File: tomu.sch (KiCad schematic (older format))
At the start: 14 parts, among them P1 DEBUG, P3 USB-PCB, U1 MKL27Z256VFM4

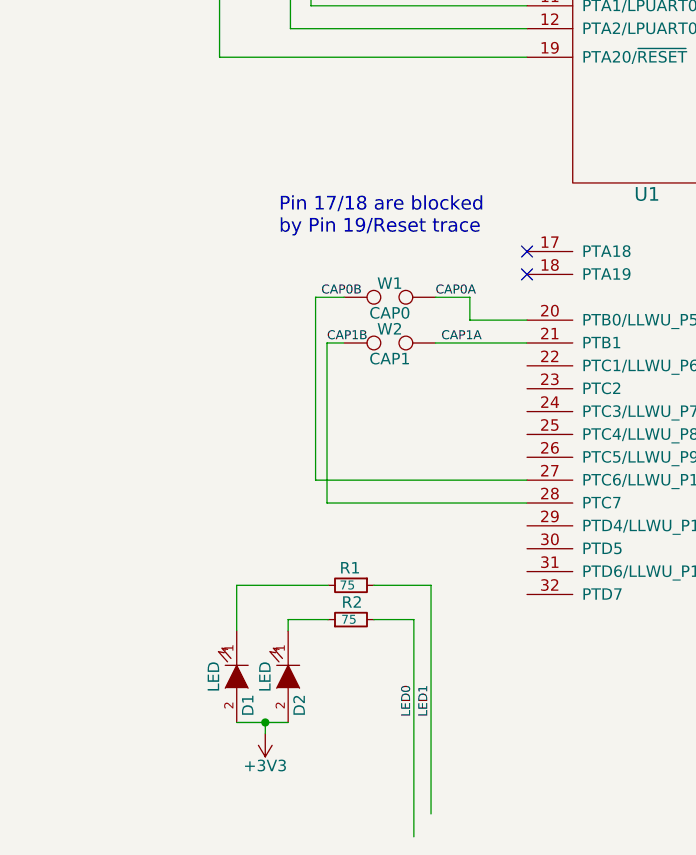
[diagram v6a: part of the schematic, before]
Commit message: Adding atecc508a part.
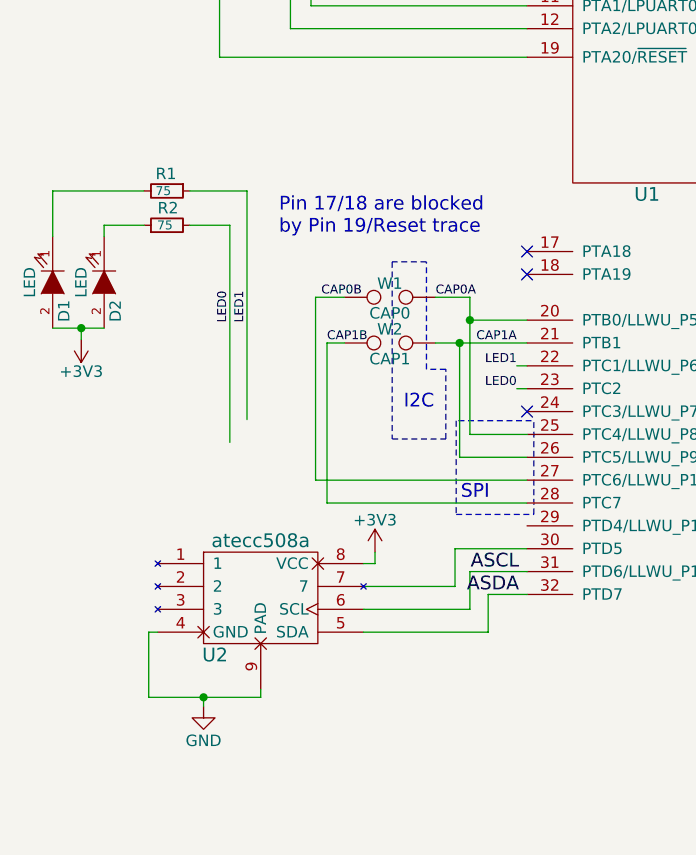
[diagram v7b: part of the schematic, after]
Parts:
- added U2: atecc508a, Housings_DFN_QFN:DFN-8-1EP_3x2mm_Pitch0.5mm, symbol atecc508a
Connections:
- net labels added: ASCL, ASDA
- wire segments 64 -> 85
- no-connect marks 2 -> 3
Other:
- note added: "I2C"
- note added: "SPI"
- moved on the sheet: D1, D2, R1, R2
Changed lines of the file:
@@
 LIBS:mkl27z265vfm4
 LIBS:usb-pcb
+LIBS:atecc508a
 LIBS:tomu-cache
 EELAYER 25 0
@@
 L LED D1
 U 1 1 5798F0D5
-P 1665 5235
-F 0 "D1" H 1790 5285 50  0000 C CNN
-F 1 "LED" H 1665 5135 50  0000 C CNN
-F 2 "LEDs:LED_0402" H 1665 5235 50  0001 C CNN
-F 3 "" H 1665 5235 50  0000 C CNN
-	1    1665 5235
+P 860 3510
+F 0 "D1" H 985 3560 50  0000 C CNN
+F 1 "LED" H 860 3410 50  0000 C CNN
+F 2 "LEDs:LED_0402" H 860 3510 50  0001 C CNN
+F 3 "" H 860 3510 50  0000 C CNN
+	1    860  3510
 	0    1    1    0
 $EndComp
@@
 L LED D2
 U 1 1 5798F173
-P 1890 5235
-F 0 "D2" H 2015 5285 50  0000 C CNN
-F 1 "LED" H 1890 5135 50  0000 C CNN
-F 2 "LEDs:LED_0402" H 1890 5235 50  0001 C CNN
-F 3 "" H 1890 5235 50  0000 C CNN
-	1    1890 5235
+P 1085 3510
+F 0 "D2" H 1210 3560 50  0000 C CNN
+F 1 "LED" H 1085 3410 50  0000 C CNN
+F 2 "LEDs:LED_0402" H 1085 3510 50  0001 C CNN
+F 3 "" H 1085 3510 50  0000 C CNN
+	1    1085 3510
 	0    1    1    0
 $EndComp
@@
 L R_Small R2
 U 1 1 5798F38A
-P 2165 4985
-F 0 "R2" V 2240 4935 50  0000 L CNN
-F 1 "75" V 2165 4960 39  0000 L CNN
-F 2 "Resistors_SMD:R_0402" H 2165 4985 50  0001 C CNN
-F 3 "" H 2165 4985 50  0000 C CNN
-	1    2165 4985
+P 1360 3260
+F 0 "R2" V 1435 3210 50  0000 L CNN
+F 1 "75" V 1360 3235 39  0000 L CNN
+F 2 "Resistors_SMD:R_0402" H 1360 3260 50  0001 C CNN
+F 3 "" H 1360 3260 50  0000 C CNN
+	1    1360 3260
 	0    -1   -1   0
 $EndComp
@@
 L R_Small R1
 U 1 1 5798F3FD
-P 2165 4835
-F 0 "R1" V 2090 4785 50  0000 L CNN
-F 1 "75" V 2165 4785 39  0000 L CNN
-F 2 "Resistors_SMD:R_0402" H 2165 4835 50  0001 C CNN
-F 3 "" H 2165 4835 50  0000 C CNN
-	1    2165 4835
+P 1360 3110
+F 0 "R1" V 1285 3060 50  0000 L CNN
+F 1 "75" V 1360 3060 39  0000 L CNN
+F 2 "Resistors_SMD:R_0402" H 1360 3110 50  0001 C CNN
+F 3 "" H 1360 3110 50  0000 C CNN
+	1    1360 3110
 	0    1    1    0
 $EndComp
@@
 F 3 "" H 2335 3775 50  0000 C CNN
 	1    2335 3775
-	1    0    0    -1
+	-1   0    0    -1
 $EndComp
 Text Notes 7045 4680 0    60   ~ 0
@@
 Text Label 2535 3575 0    39   ~ 0
 CAP0A
-Text Label 2560 3775 0    39   ~ 0
+Text Label 2890 3775 2    39   ~ 0
 CAP1A
 Text Label 1235 1725 0    39   ~ 0
@@
 Text Label 1235 1625 0    39   ~ 0
 LEU0_RX
-Text Label 2515 5410 1    39   ~ 0
+Text Label 1710 3685 1    39   ~ 0
 LED1
-Text Label 2440 5410 1    39   ~ 0
+Text Label 1635 3685 1    39   ~ 0
 LED0
 Text Label 4610 2050 0    8    ~ 0
@@
 L +3V3 #PWR05
 U 1 1 579B6568
-P 1790 5485
-F 0 "#PWR05" H 1790 5335 50  0001 C CNN
-F 1 "+3V3" H 1790 5625 50  0000 C CNN
-F 2 "" H 1790 5485 50  0000 C CNN
-F 3 "" H 1790 5485 50  0000 C CNN
-	1    1790 5485
+P 985 3760
+F 0 "#PWR05" H 985 3610 50  0001 C CNN
+F 1 "+3V3" H 985 3900 50  0000 C CNN
+F 2 "" H 985 3760 50  0000 C CNN
+F 3 "" H 985 3760 50  0000 C CNN
+	1    985  3760
 	-1   0    0    1
 $EndComp
@@
 Connection ~ 5455 3025
 Wire Wire Line
-	1790 5485 1790 5435
-Wire Wire Line
-	1665 5435 1890 5435
-Connection ~ 1790 5435
-Wire Wire Line
-	2065 4985 1890 4985
-Wire Wire Line
-	1890 4985 1890 5035
-Wire Wire Line
-	2065 4835 1665 4835
-Wire Wire Line
-	1665 4835 1665 5035
+	985  3760 985  3710
+Wire Wire Line
+	860  3710 1085 3710
+Connection ~ 985  3710
+Wire Wire Line
+	1260 3260 1085 3260
+Wire Wire Line
+	1085 3260 1085 3310
+Wire Wire Line
+	1260 3110 860  3110
+Wire Wire Line
+	860  3110 860  3310
 Wire Wire Line
 	1185 1925 1240 1925
 Wire Wire Line
-	2515 4835 2515 5835
+	1710 3110 1710 4110
 Wire Wire Line
 	2060 3775 2135 3775
@@
 	2535 3575 2685 3575
 Wire Wire Line
-	2685 3575 2685 3675
+	2685 3575 2685 4175
 Wire Wire Line
 	2685 3675 2935 3675
 Wire Wire Line
-	2535 3775 2935 3775
-Wire Wire Line
-	2515 4835 2265 4835
-Wire Wire Line
-	2440 5935 2440 4985
-Wire Wire Line
-	2440 4985 2265 4985
+	1710 3110 1460 3110
+Wire Wire Line
+	1635 4210 1635 3260
+Wire Wire Line
+	1635 3260 1460 3260
 Wire Wire Line
 	2060 3775 2060 4475
@@
 Text Notes 3930 4990 0    60   ~ 0
 ADC \n-----\n 1 - PTE0 - CMP0_OUT\n 9 - PTE30 - DAC0_OUT/ADC0_SE23/CMP0_IN4\n\n20 - PTB0 - ADC0_SE8\n21 - PTB1 - ADC0_SE9\n22 - PTC1 - ADC0_SE15\n23 - PTC2 - ADC0_SE11\n\n27 - PTC6 - CMP0_IN0\n28 - PTC7 - CMP0_IN1\n\n30 - PTD5 - ADC0_SE6b\n31 - PTD6 - ADC0_SE7b
+Wire Wire Line
+	2535 3775 2935 3775
+Text Label 2890 3875 2    39   ~ 0
+LED1
+Text Label 2890 3975 2    39   ~ 0
+LED0
+Wire Wire Line
+	2935 3975 2890 3975
+Wire Wire Line
+	2935 3875 2890 3875
+Wire Notes Line
+	2345 3420 2345 4195
+Wire Notes Line
+	2345 4195 2580 4195
+Wire Notes Line
+	2580 4195 2580 3890
+Wire Notes Line
+	2580 3890 2495 3890
+Wire Notes Line
+	2495 3890 2495 3420
+Wire Notes Line
+	2495 3420 2345 3420
+Text Notes 2395 4070 0    60   ~ 0
+I2C
+Wire Notes Line
+	2955 4115 2625 4115
+Wire Notes Line
+	2625 4115 2625 4525
+Wire Notes Line
+	2625 4525 2965 4525
+Wire Notes Line
+	2965 4525 2965 4115
+Text Notes 2645 4465 0    60   ~ 0
+SPI
+Wire Wire Line
+	2935 4275 2640 4275
+Wire Wire Line
+	2640 4275 2640 3775
+Connection ~ 2640 3775
+Wire Wire Line
+	2685 4175 2935 4175
+Connection ~ 2685 3675
+NoConn ~ 2935 4075
+$Comp
+L atecc508a U2
+U 1 1 58384DF6
+P 1520 5040
+F 0 "U2" H 1570 4940 60  0000 C CNN
+F 1 "atecc508a" H 1770 5440 60  0000 C CNN
+F 2 "Housings_DFN_QFN:DFN-8-1EP_3x2mm_Pitch0.5mm" H 1520 5040 60  0001 C CNN
+F 3 "" H 1520 5040 60  0001 C CNN
+	1    1520 5040
+	1    0    0    -1
+$EndComp
+Wire Wire Line
+	1770 5290 1770 5325
+Wire Wire Line
+	1770 5325 1280 5325
+Wire Wire Line
+	1280 5325 1280 5040
+Wire Wire Line
+	1280 5040 1320 5040
+$Comp
+L GND #PWR07
+U 1 1 583859AA
+P 1520 5365
+F 0 "#PWR07" H 1520 5115 50  0001 C CNN
+F 1 "GND" H 1520 5215 50  0000 C CNN
+F 2 "" H 1520 5365 50  0000 C CNN
+F 3 "" H 1520 5365 50  0000 C CNN
+	1    1520 5365
+	1    0    0    -1
+$EndComp
+Wire Wire Line
+	1520 5365 1520 5325
+Connection ~ 1520 5325
+Wire Wire Line
+	2220 4740 2270 4740
+Wire Wire Line
+	2270 4740 2270 4690
+$Comp
+L +3V3 #PWR08
+U 1 1 58385F9E
+P 2270 4690
+F 0 "#PWR08" H 2270 4540 50  0001 C CNN
+F 1 "+3V3" H 2270 4830 50  0000 C CNN
+F 2 "" H 2270 4690 50  0000 C CNN
+F 3 "" H 2270 4690 50  0000 C CNN
+	1    2270 4690
+	1    0    0    -1
+$EndComp
+Wire Wire Line
+	2220 5040 2765 5040
+Wire Wire Line
+	2765 5040 2765 4875
+Wire Wire Line
+	2765 4875 2935 4875
+Wire Wire Line
+	2220 4940 2685 4940
+Wire Wire Line
+	2685 4940 2685 4775
+Wire Wire Line
+	2685 4775 2935 4775
+Wire Wire Line
+	2215 4840 2620 4840
+Wire Wire Line
+	2620 4840 2620 4675
+Wire Wire Line
+	2620 4675 2935 4675
+Text Label 2900 4775 2    60   ~ 0
+ASCL
+Text Label 2900 4875 2    60   ~ 0
+ASDA
 $EndSCHEMATC

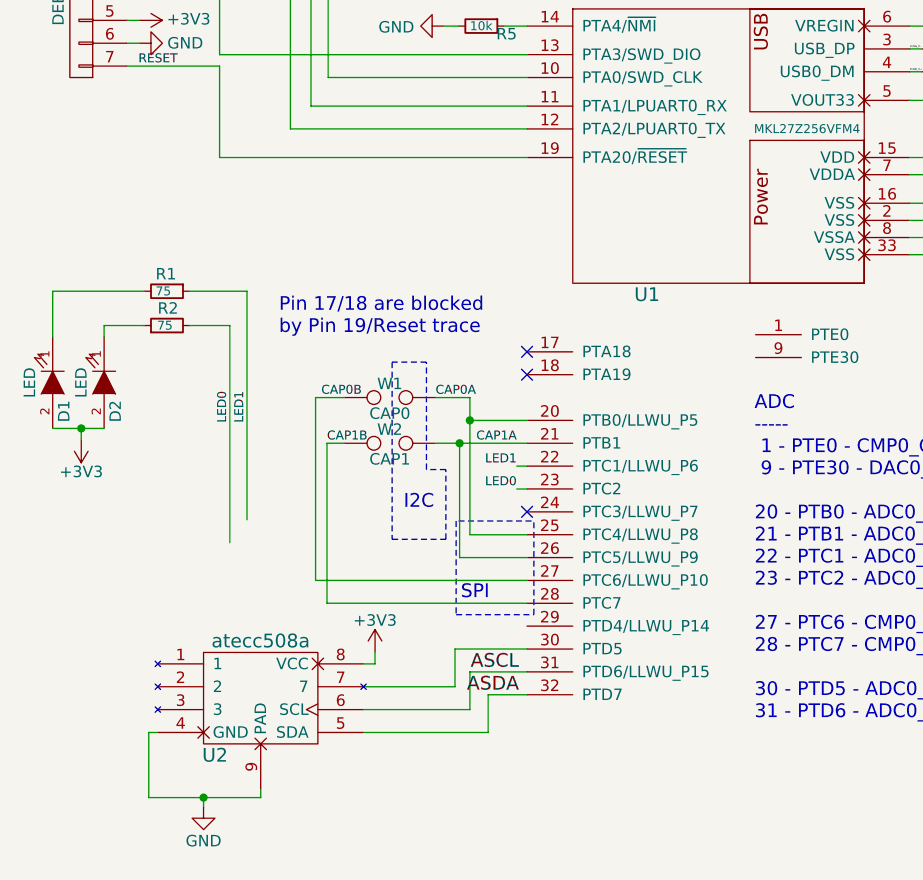
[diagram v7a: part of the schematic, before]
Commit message: Allow any of the ATECC parts.
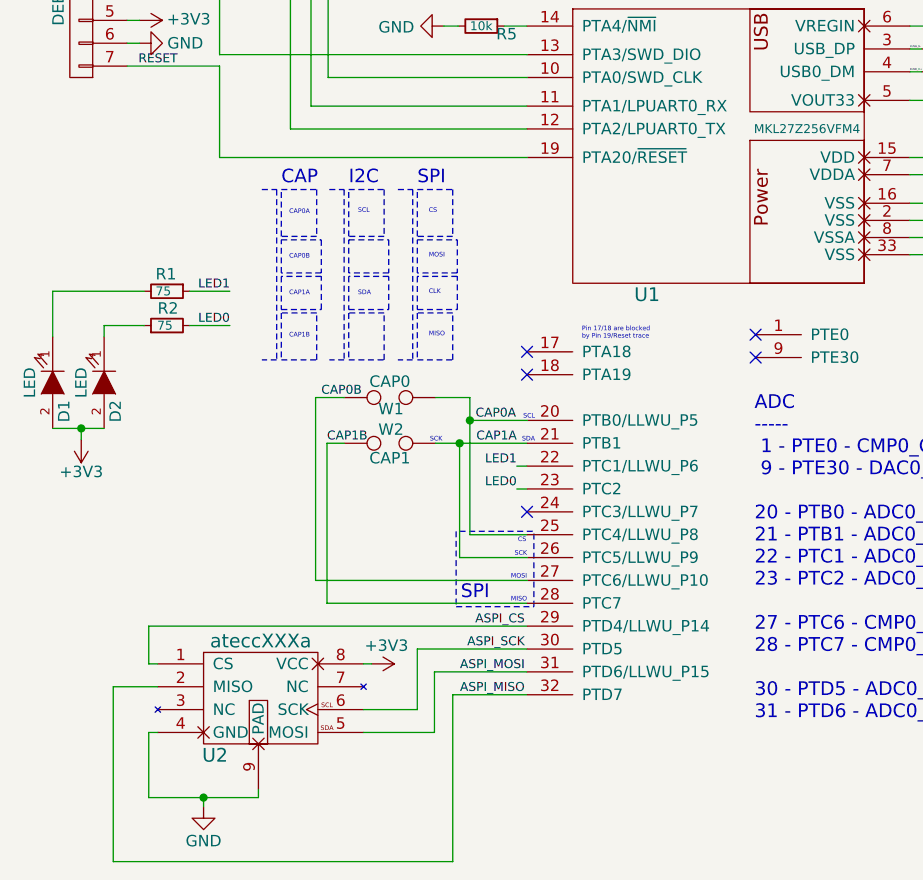
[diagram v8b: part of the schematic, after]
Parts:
- removed U2: atecc508a, Housings_DFN_QFN:DFN-8-1EP_3x2mm_Pitch0.5mm, symbol atecc508a
- added U2: ateccXXXa, symbol ateccXXXa
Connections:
- net labels added: ASPI_CS, ASPI_MISO, ASPI_MOSI, ASPI_SCK
- net labels removed: ASCL, ASDA
- wire segments 85 -> 87
- no-connect marks 3 -> 5
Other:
- note added: "CAP"
- note added: "CAP0A"
- note added: "CAP0B"
- note added: "CAP1A"
- note added: "CAP1B"
- note added: "CLK"
- note added: "CS"
- note added: "MISO"
- note added: "MOSI"
- note added: "SCK"
- note added: "SCL"
- note added: "SDA"
